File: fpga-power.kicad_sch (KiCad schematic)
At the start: 100 parts, among them U4 XC7K160T-FFG676

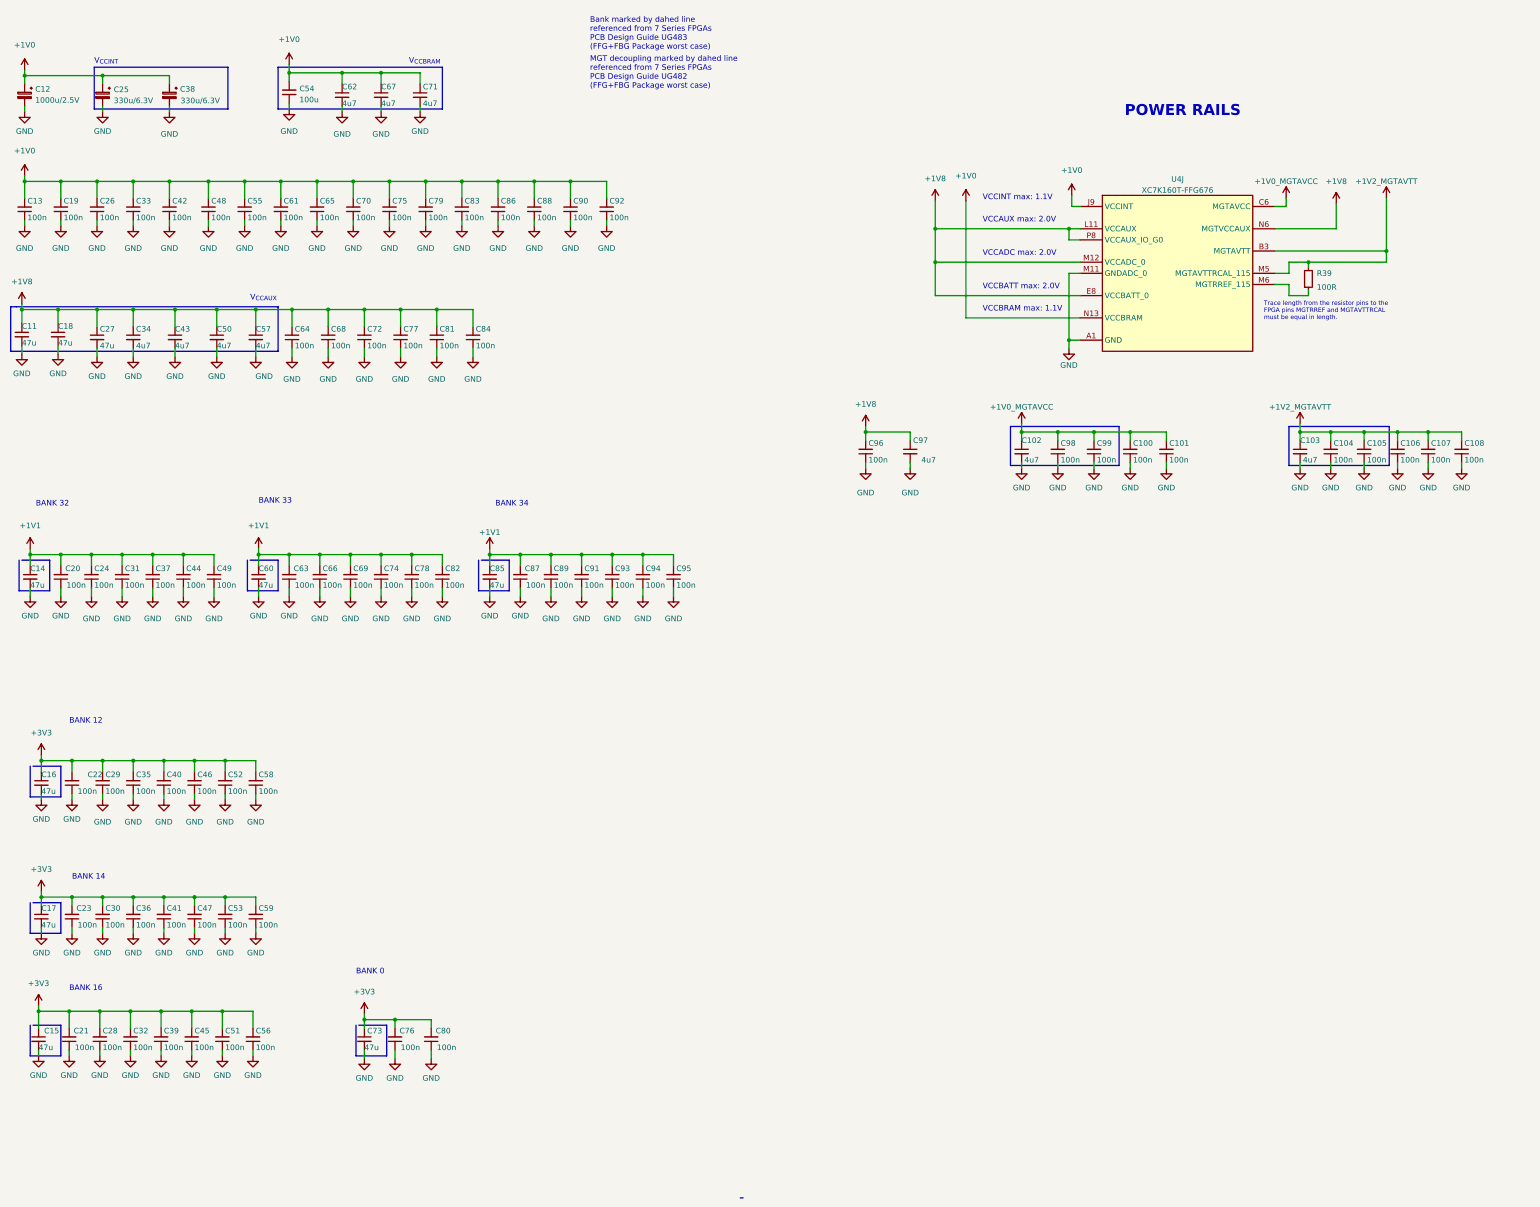
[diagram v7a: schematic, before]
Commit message: Finish updating components to newest versions, improve silkscreen marking, bump revision
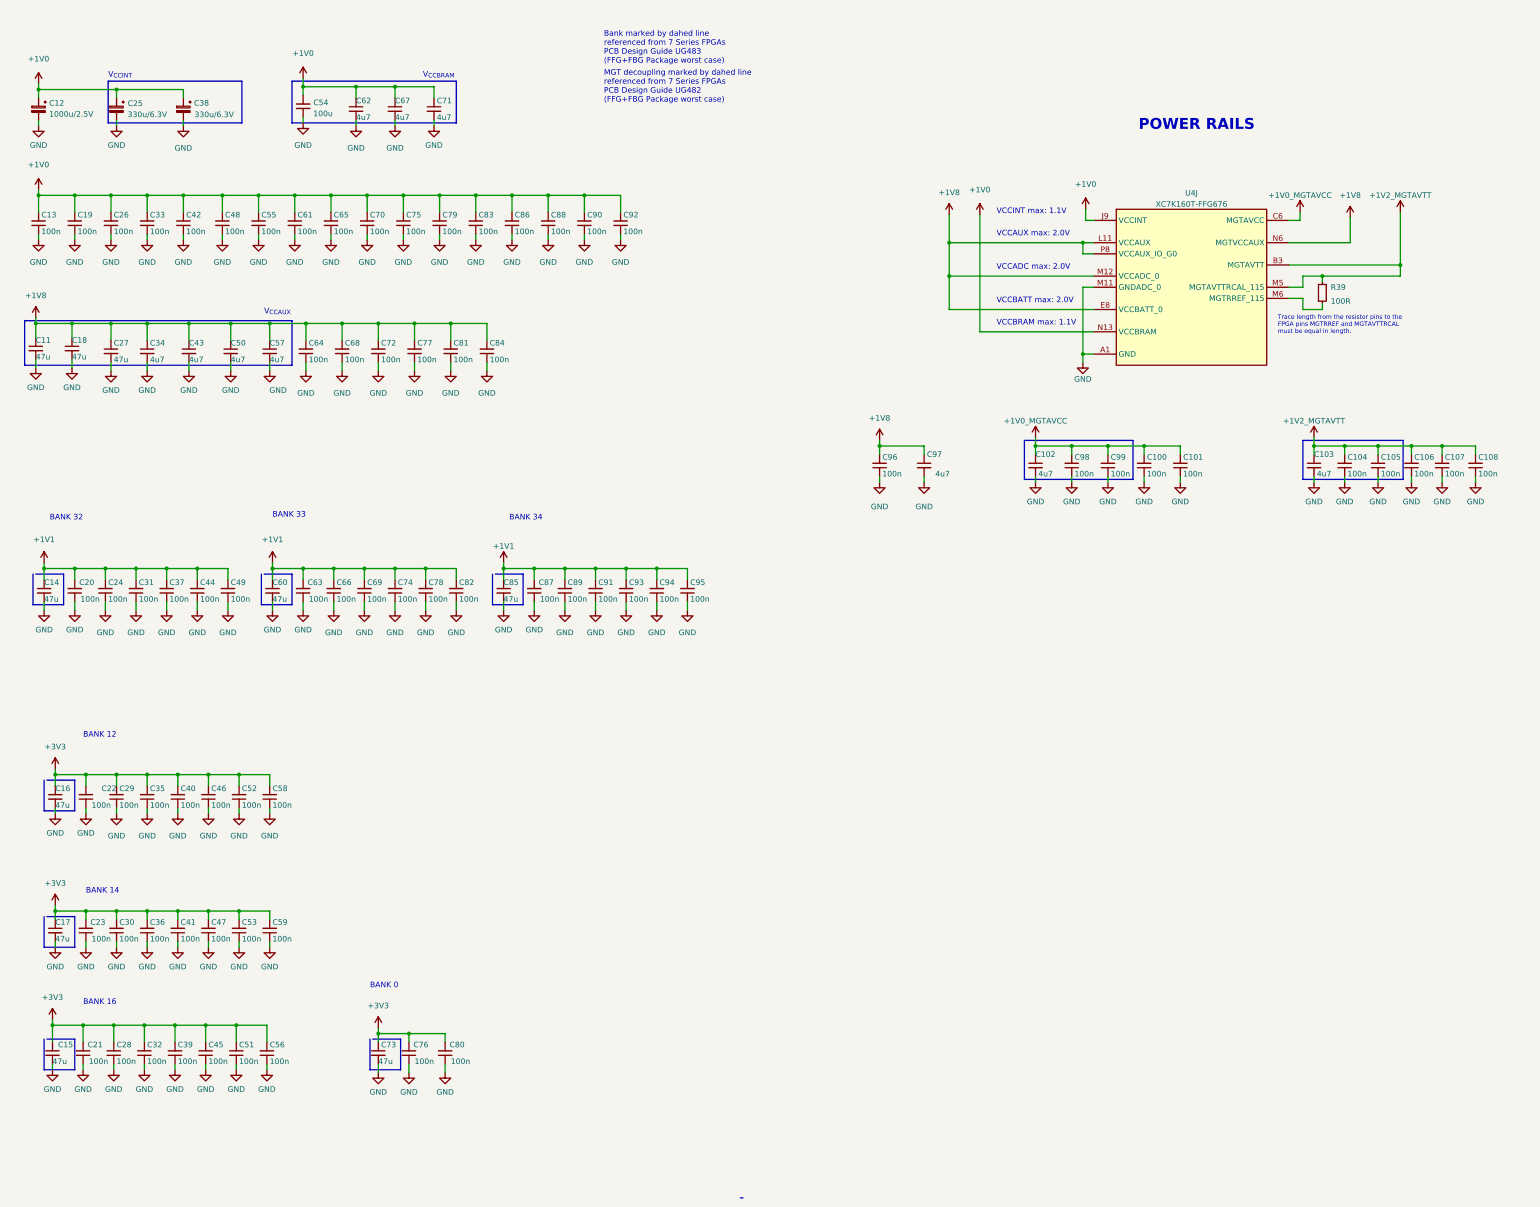
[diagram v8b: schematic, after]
